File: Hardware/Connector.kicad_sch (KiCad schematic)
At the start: 6 parts, among them J1 Conn_02x16_Counter_Clockwise, J2 FTSH-107-01-L-D-K

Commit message: Changes in CAN section
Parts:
- added D6, D7: 5.3V/400W, Package_TO_SOT_SMD:SOT-23-3, symbol Power_Protection:ESDA5V3L
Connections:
- net CAN1+: now also D7.1 (K)
- net CAN1-: now also D7.2 (K)
- net CAN2+: now also D6.1 (K)
- net CAN2-: now also D6.2 (K)
- new net GND_CAN_ISO: D6.3 (A), D7.3 (A)

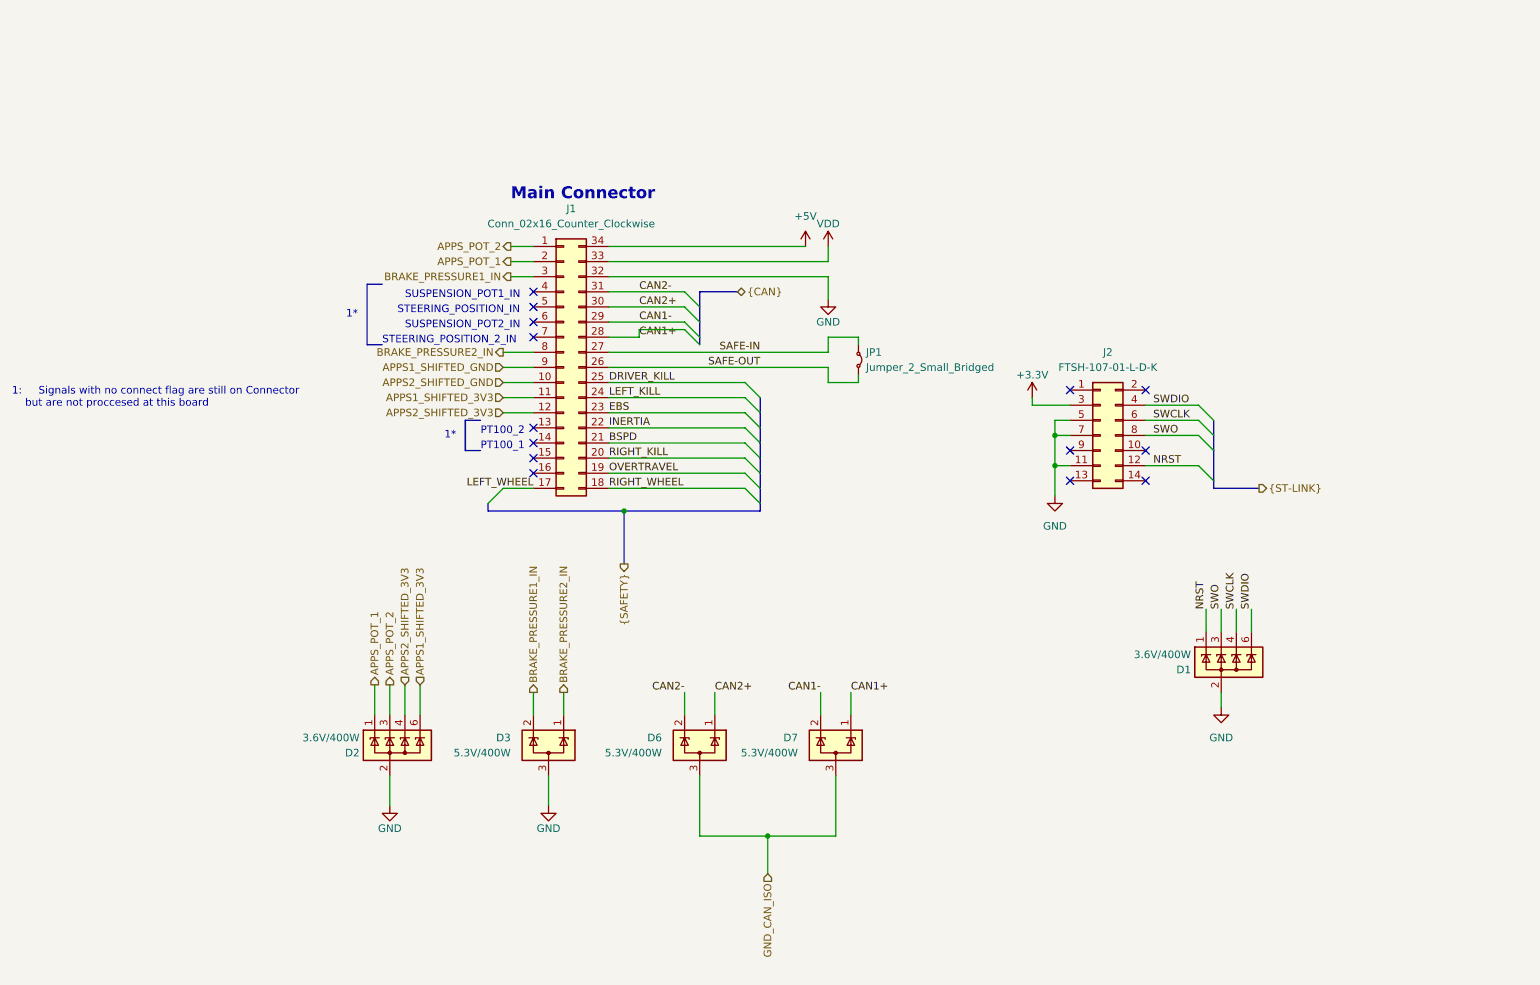
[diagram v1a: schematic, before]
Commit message: Changes in schematic, separated CAN buses, added XIAO Sense S3 DevBoard
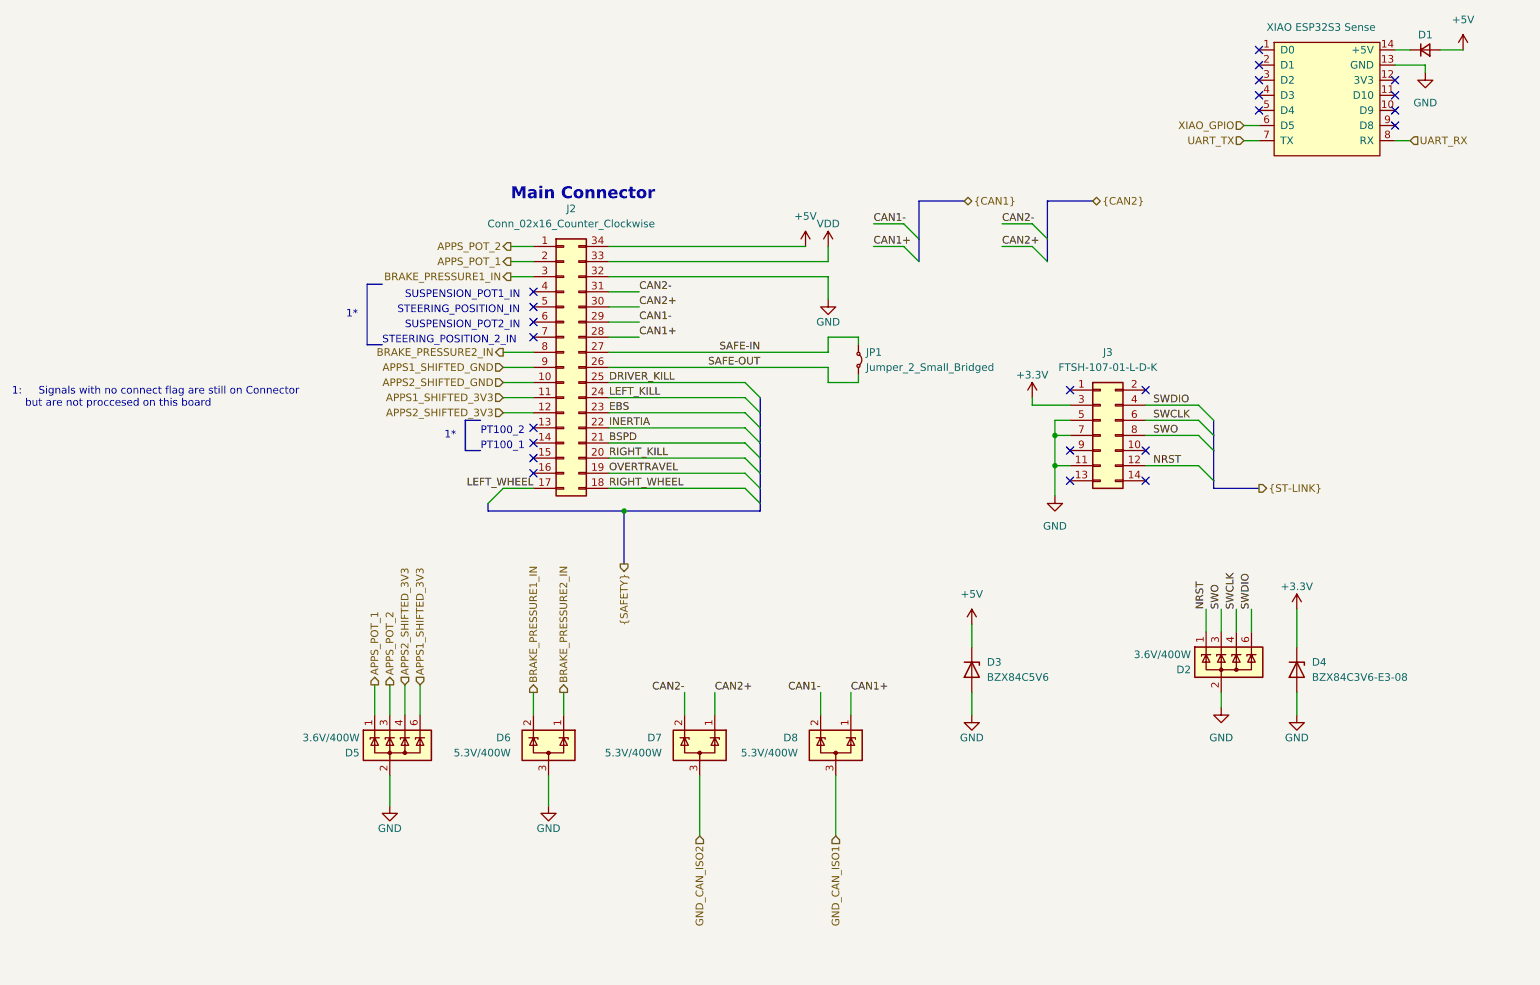
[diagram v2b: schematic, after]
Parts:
- added D1: NSVRB751V40T1G, Diode_SMD:D_SOD-323_HandSoldering, symbol Device:D_Small
- added D3: BZX84C5V6, Package_TO_SOT_SMD:SOT-23, symbol Diode:BZX84Cxx
- added D4: BZX84C3V6-E3-08, Package_TO_SOT_SMD:SOT-23, symbol Diode:BZX84Cxx
- added J1: XIAO ESP32S3 Sense, Samacsys:XIAO-ESP32S3-DIP, symbol Connector:Conn_01x04_Socket
- renumbered D1 to D2, D2 to D5, D3 to D6, D6 to D7, D7 to D8, J1 to J2, J2 to J3
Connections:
- net +3.3V: now also D4.3 (K)
- net +5V: now also D1.2 (A), D3.3 (K)
- net GND: now also D3.1 (A), D4.1 (A), J1.13 (GND)
- net GND_CAN_ISO renamed GND_CAN_ISO1
- net GND_CAN_ISO1: no longer D7.3 (A)
- new net: D1.1 (K), J1.14 (+5V)
- new net GND_CAN_ISO2: D7.3 (A)
- new net UART_RX: J1.8 (RX)
- new net UART_TX: J1.7 (TX)
- new net XIAO_GPIO: J1.6 (D5)
- no-connect marks 14 -> 23
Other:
- note added: "1: Signals with no connect flag are still on Connector but are not proccesed on this board"
- note removed: "1: Signals with no connect flag are still on Connector but are not proccesed at this board"

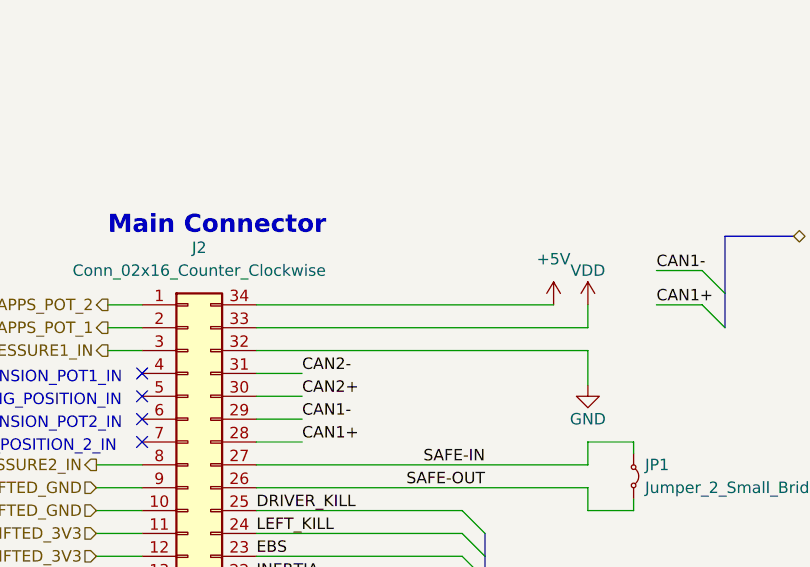
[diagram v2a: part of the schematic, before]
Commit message: Added fuse to external 5V power supply
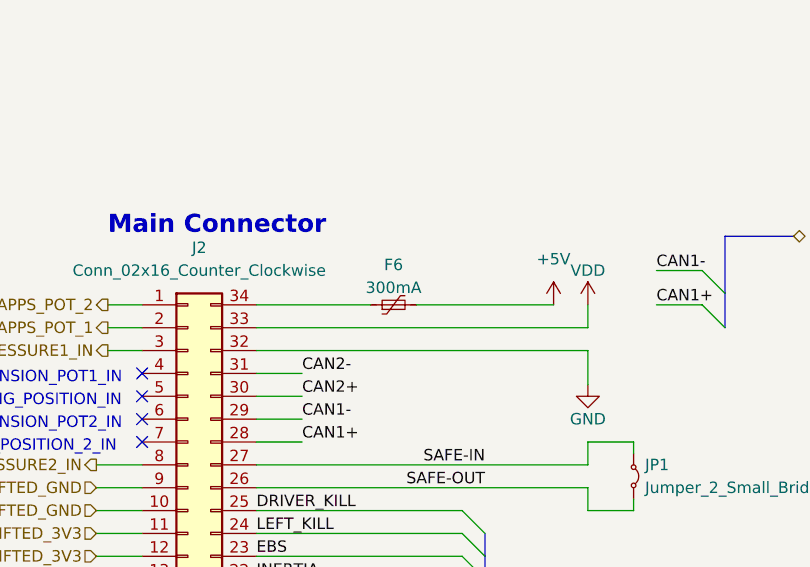
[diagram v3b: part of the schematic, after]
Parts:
- added F6: 300mA, Fuse:Fuse_0603_1608Metric_Pad1.05x0.95mm_HandSolder, symbol Device:Polyfuse_Small
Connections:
- net +5V: now also F6.2; no longer J2.34 (Pin_34)
- new net: F6.1, J2.34 (Pin_34)
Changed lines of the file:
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@@
+		)
+	)
+	(wire
+		(pts
+			(xy 129.54 72.39) (xy 142.24 72.39)
+		)
+		(stroke
+			(width 0)
+			(type default)
 		)
 	)
@@
 	(wire
 		(pts
-			(xy 129.54 72.39) (xy 162.56 72.39)
-		)
-		(stroke
-			(width 0)
-			(type default)
-		)
-	)
-	(wire
-		(pts
 			(xy 166.37 77.47) (xy 166.37 81.28)
 		)
@@
 		(pts
 			(xy 95.25 151.13) (xy 95.25 146.05)
+		)
+		(stroke
+			(width 0)
+			(type default)
+		)
+	)
+	(wire
+		(pts
+			(xy 147.32 72.39) (xy 162.56 72.39)
 		)
 		(stroke
@@
 					(unit 1)
 				)
+			)
+		)
+	)
+	(symbol
+		(lib_id "Device:Polyfuse_Small")
+		(at 144.78 72.39 90)
+		(unit 1)
+		(exclude_from_sim no)
+		(in_bom yes)
+		(on_board yes)
+		(dnp no)
+		(fields_autoplaced yes)
+		(property "Reference" "F6"
+			(at 144.78 67.945 90)
+			(effects
+				(font
+					(size 1.27 1.27)
+				)
+			)
+		)
+		(property "Value" "300mA"
+			(at 144.78 70.485 90)
+			(effects
+				(font
+					(size 1.27 1.27)
+				)
+			)
+		)
+		(property "Footprint" "Fuse:Fuse_0603_1608Metric_Pad1.05x0.95mm_HandSolder"
+			(at 149.86 71.12 0)
+			(effects
+				(font
+					(size 1.27 1.27)
+				)
+				(justify left)
+				(hide yes)
+			)
+		)
+		(property "Datasheet" "https://www.mouser.pl/datasheet/2/447/YAGO_S_A0011407805_1-2572780.pdf"
+			(at 144.78 72.39 0)
+			(effects
+				(font
+					(size 1.27 1.27)
+				)
+				(hide yes)
+			)
+		)
+		(property "Description" "SMD0603B010TF"
+			(at 144.78 72.39 0)
+			(effects
+				(font
+					(size 1.27 1.27)
+				)
+				(hide yes)
+			)
+		)
+		(pin "1"
+		)
+		(pin "2"
+		)
+		(instances
+			(project "PUTM_EV_Frontbox"
+				(path "/b652b05a-4e3d-4ad1-b032-18886abe7d45/05ab4043-b566-4501-8a33-377ac21fdb45"
+					(reference "F6")
+					(unit 1)
+				)

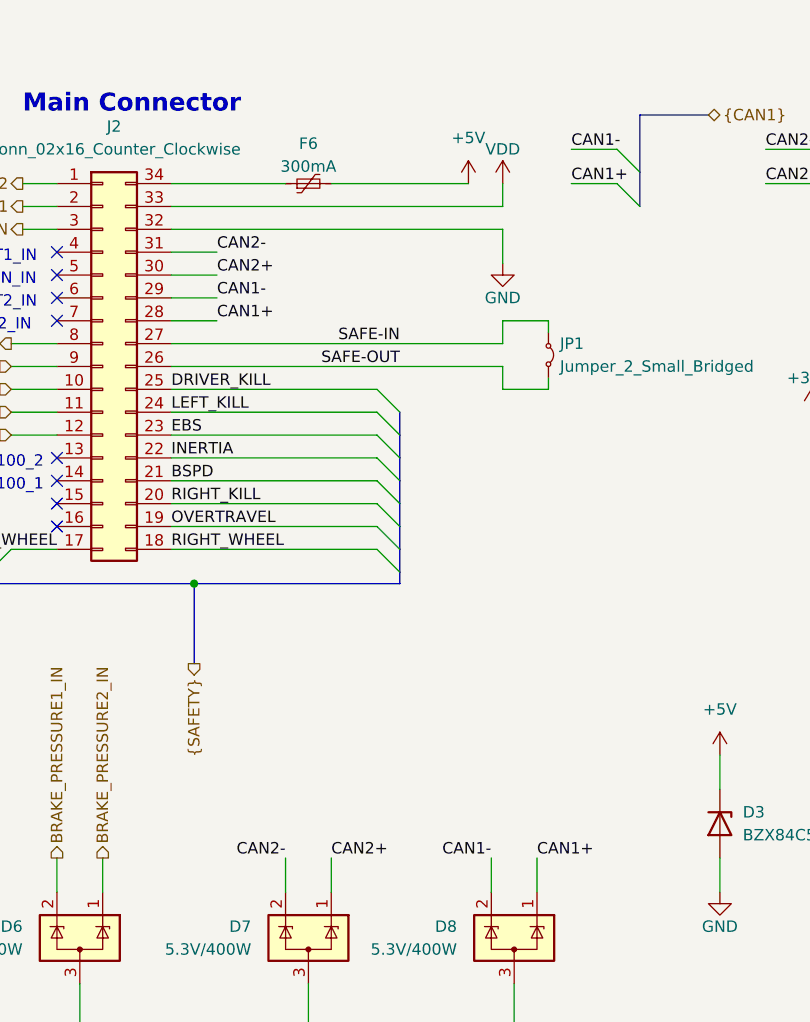
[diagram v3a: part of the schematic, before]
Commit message: Initial layout, changes in safety sensing bus labels
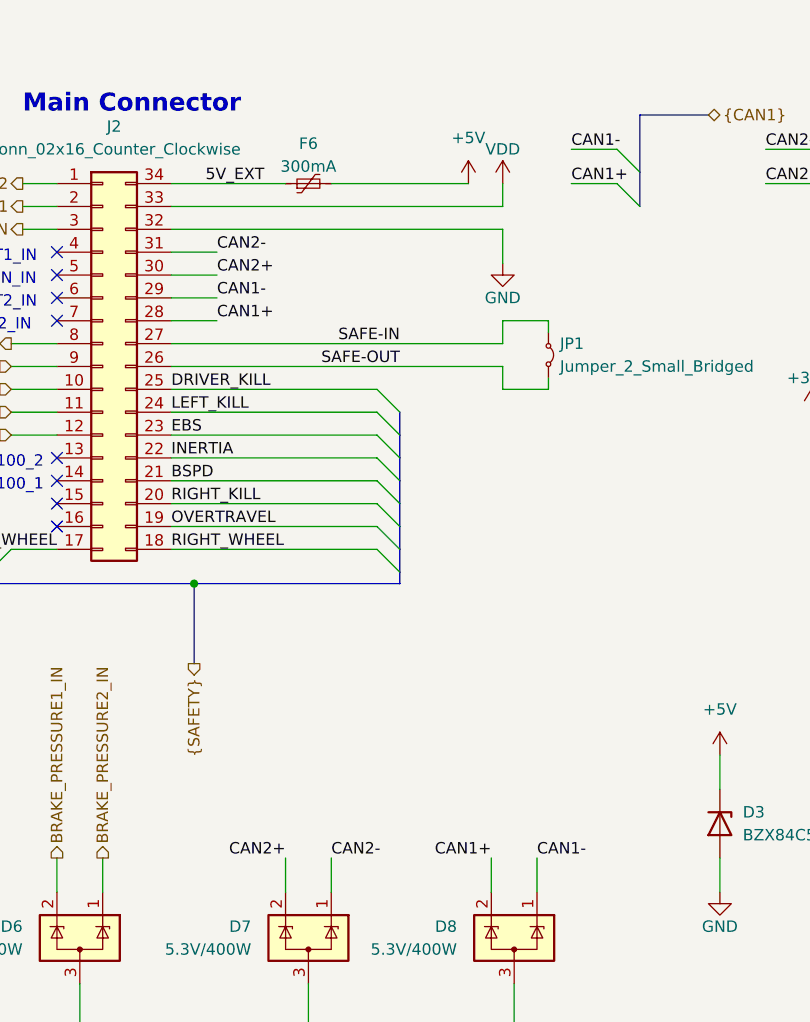
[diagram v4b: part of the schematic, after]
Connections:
- net CAN1+: now also D8.2 (K); no longer D8.1 (K)
- net CAN1-: now also D8.1 (K); no longer D8.2 (K)
- net CAN2+: now also D7.2 (K); no longer D7.1 (K)
- net CAN2-: now also D7.1 (K); no longer D7.2 (K)
- net 5V_EXT: now reaches F6.1, J2.34 (Pin_34)

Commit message: Initial routing (Piotruś proszę nie bij że brzydko)
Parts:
- removed D7, D8: 5.3V/400W, Package_TO_SOT_SMD:SOT-23-3, symbol Power_Protection:ESDA5V3L
- added D15: 3.6V/400W, Package_TO_SOT_SMD:SOT-23-6, symbol Power_Protection:ESDA5V3SC5
- added D7, D8: PESD5V0L2BT, Package_TO_SOT_SMD:SOT-23_Handsoldering, symbol Device:D_TVS_Dual_AAC
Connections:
- net CAN1+: now also D8.1 (A1)
- net CAN1-: now also D8.2 (A2)
- net CAN2+: now also D7.1 (A1)
- net CAN2-: now also D7.2 (A2)
- net GND: now also D15.2 (K), D15.5 (NC)
- net GND_CAN_ISO1: now also D8.3 (common)
- net GND_CAN_ISO2: now also D7.3 (common)
- net UART_RX: now also D15.1 (A)
- net UART_TX: now also D15.3 (A)
- net UART_RX_PROG: now reaches J3.13 (Pin_13)
- net UART_RX_PROG: now also D15.4 (A)
- net UART_TX_PROG: now reaches J3.14 (Pin_14)
- net UART_TX_PROG: now also D15.6 (A)
- no-connect marks 23 -> 21

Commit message: Changes in CAN section
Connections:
- net +5V: no longer D3.3 (K)
- net 5V_EXT: now also D3.3 (K)
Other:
- title: (none) -> FrontBox
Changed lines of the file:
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@@
 	(generator_version "9.0")
 	(paper "A4")
+	(title_block
+		(title "FrontBox")
+	)
 	(bus_alias "CAN1"
 		(members "CAN1-" "CAN1+")
@@
 	(label "CAN2-"
 		(at 148.59 149.86 0)
+		(effects
+			(font
+				(size 1.27 1.27)
+			)
+			(justify left bottom)
+		)
+	)
+	(label "5V_EXT"
+		(at 190.5 135.89 0)
 		(effects
 			(font
@@
 					(unit 1)
 				)
-			)
-		)
-	)
-	(symbol
-		(lib_id "power:+5V")
-		(at 190.5 135.89 0)
-		(unit 1)
-		(exclude_from_sim no)
-		(in_bom yes)
-		(on_board yes)
-		(dnp no)
-		(property "Reference" "#PWR09"
-			(at 190.5 139.7 0)
-			(effects
-				(font
-					(size 1.27 1.27)
-				)
-				(hide yes)
-			)
-		)
-		(property "Value" "+5V"
-			(at 190.5 130.81 0)
-			(effects
-				(font
-					(size 1.27 1.27)
-				)
-			)
-		)
-		(property "Footprint" ""
-			(at 190.5 135.89 0)
-			(effects
-				(font
-					(size 1.27 1.27)
-				)
-				(hide yes)
-			)
-		)
-		(property "Datasheet" ""
-			(at 190.5 135.89 0)
-			(effects
-				(font
-					(size 1.27 1.27)
-				)
-				(hide yes)
-			)
-		)
-		(property "Description" ""
-			(at 190.5 135.89 0)
-			(effects
-				(font
-					(size 1.27 1.27)
-				)
-				(hide yes)
-			)
-		)
-		(pin "1"
-		)
-		(instances
-			(project "PUTM_EV_Frontbox"
-				(path "/b652b05a-4e3d-4ad1-b032-18886abe7d45/05ab4043-b566-4501-8a33-377ac21fdb45"
-					(reference "#PWR09")
-					(unit 1)
-				)

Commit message: BOM update
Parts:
- D3: Mouser Part Number (none) -> 637-BZX84C5V6
- D4: Mouser Part Number (none) -> 78-BZX84C3V6-E3-08
- D7, D8: Mouser Part Number (none) -> 771-PESD5V0L2BT-QR
- F6, J1, J2, JP1: Mouser Part Number (none) -> .
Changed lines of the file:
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@@
+			)
+		)
+		(property "Mouser Part Number" "771-PESD5V0L2BT-QR"
+			(at 139.7 153.67 0)
+			(effects
+				(font
+					(size 1.27 1.27)
+				)
+				(hide yes)
 			)
 		)
@@
 			)
 		)
+		(property "Mouser Part Number" "771-PESD5V0L2BT-QR"
+			(at 171.45 153.67 0)
+			(effects
+				(font
+					(size 1.27 1.27)
+				)
+				(hide yes)
+			)
+		)
 		(pin "1"
 		)
@@
 			)
 		)
+		(property "Mouser Part Number" "78-BZX84C3V6-E3-08"
+			(at 245.11 143.51 0)
+			(effects
+				(font
+					(size 1.27 1.27)
+				)
+				(hide yes)
+			)
+		)
 		(pin "1"
 		)
@@
 			)
 		)
+		(property "Mouser Part Number" "."
+			(at 144.78 72.39 0)
+			(effects
+				(font
+					(size 1.27 1.27)
+				)
+			)
+		)
 		(pin "1"
 		)
@@
 			)
 		)
+		(property "Mouser Part Number" "."
+			(at 171.45 91.44 0)
+			(effects
+				(font
+					(size 1.27 1.27)
+				)
+			)
+		)
 		(pin "1"
 		)
@@
 			)
 		)
+		(property "Mouser Part Number" "."
+			(at 121.92 92.71 0)
+			(effects
+				(font
+					(size 1.27 1.27)
+				)
+			)
+		)
 		(pin "1"
 		)
@@
 			)
 		)
+		(property "Mouser Part Number" "637-BZX84C5V6"
+			(at 190.5 143.51 0)
+			(effects
+				(font
+					(size 1.27 1.27)
+				)
+				(hide yes)
+			)
+		)
 		(pin "1"
 		)
@@
 			)
 		)
+		(property "Mouser Part Number" "."
+			(at 250.19 48.26 0)
+			(effects
+				(font
+					(size 1.27 1.27)
+				)
+			)
+		)

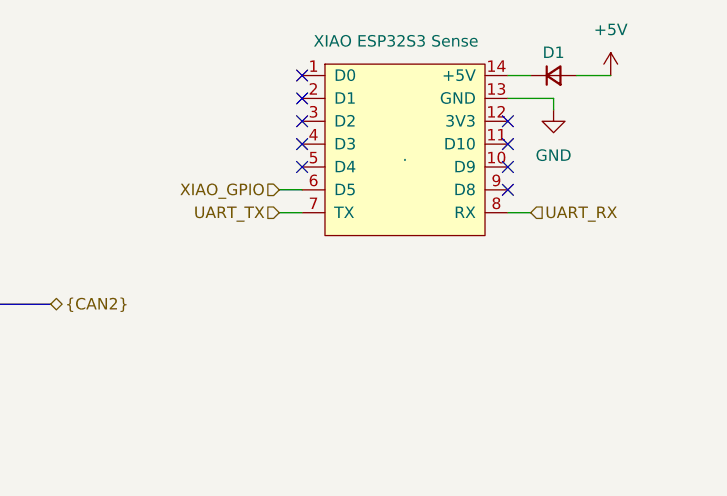
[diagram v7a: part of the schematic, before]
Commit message: Silkscreen changes
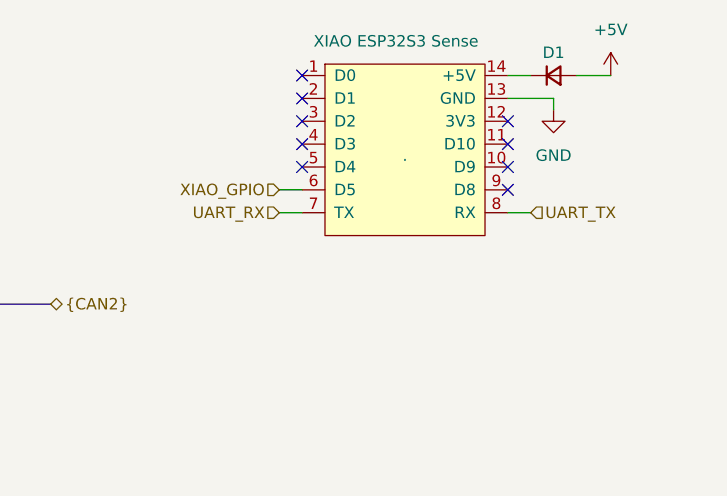
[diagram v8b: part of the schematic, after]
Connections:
- net UART_RX: now also J1.7 (TX); no longer J1.8 (RX)
- net UART_TX: now also J1.8 (RX); no longer J1.7 (TX)
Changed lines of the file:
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@@
+	(wire
+		(pts
+			(xy 261.62 54.61) (xy 264.16 54.61)
+		)
+		(stroke
+			(width 0)
+			(type default)
+		)
+	)
 	(wire
 		(pts
@@
 	(wire
 		(pts
+			(xy 236.22 54.61) (xy 238.76 54.61)
+		)
+		(stroke
+			(width 0)
+			(type default)
+		)
+	)
+	(wire
+		(pts
 			(xy 232.41 147.32) (xy 232.41 149.86)
 		)
@@
 	(wire
 		(pts
-			(xy 236.22 54.61) (xy 238.76 54.61)
-		)
-		(stroke
-			(width 0)
-			(type default)
-		)
-	)
-	(wire
-		(pts
 			(xy 204.47 111.76) (xy 207.01 111.76)
 		)
@@
 		(pts
 			(xy 203.2 74.93) (xy 203.2 71.12)
-		)
-		(stroke
-			(width 0)
-			(type default)
-		)
-	)
-	(wire
-		(pts
-			(xy 264.16 54.61) (xy 261.62 54.61)
 		)
 		(stroke
@@
 	(hierarchical_label "UART_TX"
 		(shape input)
-		(at 236.22 54.61 180)
-		(effects
-			(font
-				(size 1.27 1.27)
-			)
-			(justify right)
+		(at 264.16 54.61 0)
+		(effects
+			(font
+				(size 1.27 1.27)
+			)
+			(justify left)
 		)
 	)
@@
 	(hierarchical_label "UART_RX"
 		(shape input)
-		(at 264.16 54.61 0)
-		(effects
-			(font
-				(size 1.27 1.27)
-			)
-			(justify left)
-		)
-	)
+		(at 236.22 54.61 180)
+		(effects
+			(font
+				(size 1.27 1.27)
+			)
+			(justify right)
+		)
+	)
